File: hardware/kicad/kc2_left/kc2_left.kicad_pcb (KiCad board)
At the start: 2 copper layers, 146.4 x 133.8 mm, 70 parts, among them SW1 KEY_01, SW10 KEY_10, SW11 KEY_11, SW12 KEY_12, SW13 KEY_13, SW14 KEY_14, SW15 KEY_15, SW16 KEY_16, SW17 KEY_17, SW18 KEY_18, SW19 KEY_19, SW2 KEY_02, SW20 KEY_20, SW21 KEY_21, SW22 KEY_22, SW23 KEY_23, SW24 KEY_24, SW25 KEY_25, SW26 KEY_26, SW27 KEY_27, SW28 KEY_28, SW29 KEY_29, SW3 KEY_03, SW30 KEY_30, SW4 KEY_04, SW5 KEY_05, SW6 KEY_06, SW7 KEY_07, SW8 KEY_08, SW9 KEY_09, U1 nice!nano_v2_socket_24pin

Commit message: Finalize KC2 routed PCB draft
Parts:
- moved H3 1.00 mm to (115.4, 44.0)
- moved H4 1.00 mm to (151.4, 44.0)
- moved J_PWR1 1.00 mm to (105.4, 50.0)
- moved SW_RST1 1.00 mm to (123.5, 62.1)
- moved U1 1.00 mm to (133.4, 49.0)
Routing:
- net L_COL3: track 176.2 -> 146.8 mm, vias 1 -> 0
- net L_COL2: track 190.5 -> 165.8 mm, vias 1 -> 0
- net L_COL0: track 219.3 -> 195.5 mm, vias 1 -> 0
- net L_ROW2: track 177.0 -> 157.6 mm, vias 7 -> 1
- net L_ROW0: track 149.6 -> 131.4 mm, vias 7 -> 0
- net L_COL1: track 208.7 -> 191.7 mm
- net L_ROW3: track 199.7 -> 184.4 mm, vias 6 -> 1
- net L_COL4: track 152.7 -> 139.1 mm, vias 1 -> 0
- net L_COL5: track 126.4 -> 112.9 mm
- net L_ROW1: track 150.2 -> 137.0 mm, vias 6 -> 1
- net L_ROW4: track 203.9 -> 211.2 mm, vias 6 -> 1
- net LK15_D: track 15.4 -> 12.0 mm, vias 1 -> 0
- net L_COL6: track 53.5 -> 50.3 mm
- net LK30_D: track 12.0 -> 15.0 mm, vias 0 -> 1
- net LK23_D: track 12.0 -> 13.6 mm
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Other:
- outline, holes or cut-outs redrawn

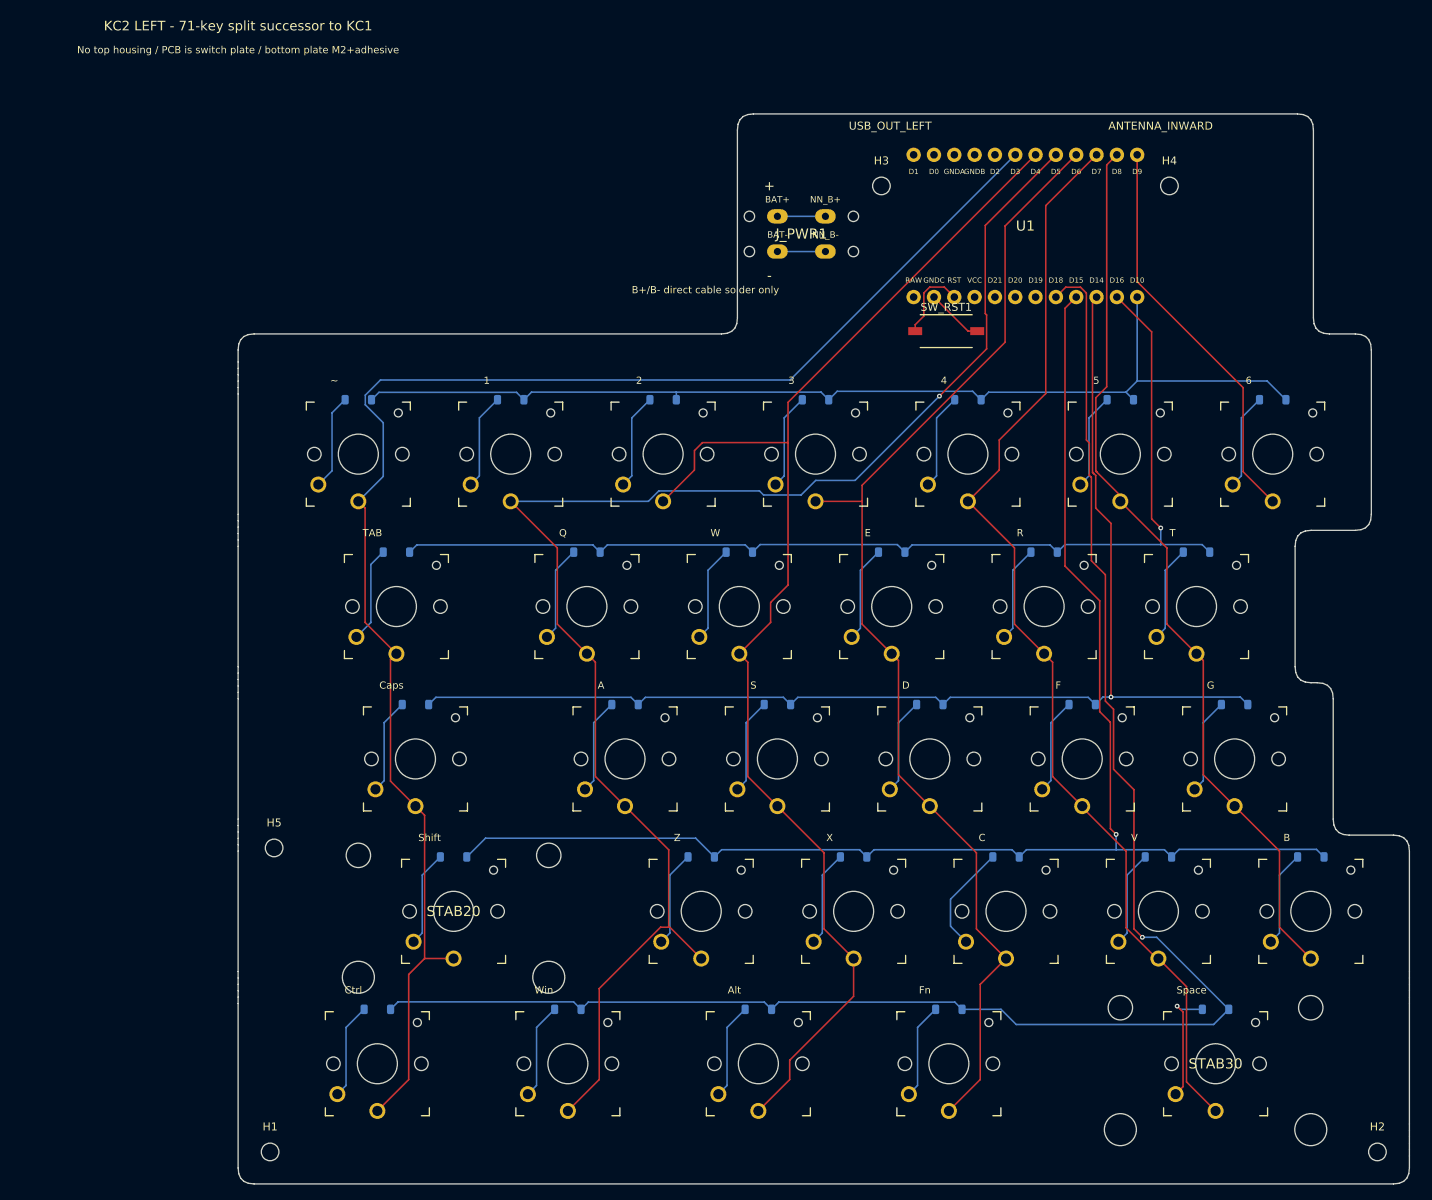
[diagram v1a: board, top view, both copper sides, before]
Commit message: chore: OPS-ARCH-002 KC2 X3 KiCad 산출물을 main 경로로 승격한다
- X3 좌우 프로젝트를 hardware/kicad/kc2_left, hardware/kicad/kc2_right로 승격
- soldered, hotswap, x1, x2 변형은 hardware/kicad/draft 아래에 보존
- manifest, autoroute, file naming, fabrication ZIP, renders, verify scripts를 main 경로 기준으로 갱신
- SRS evidence와 OPS-ARCH-002 verified 상태를 반영
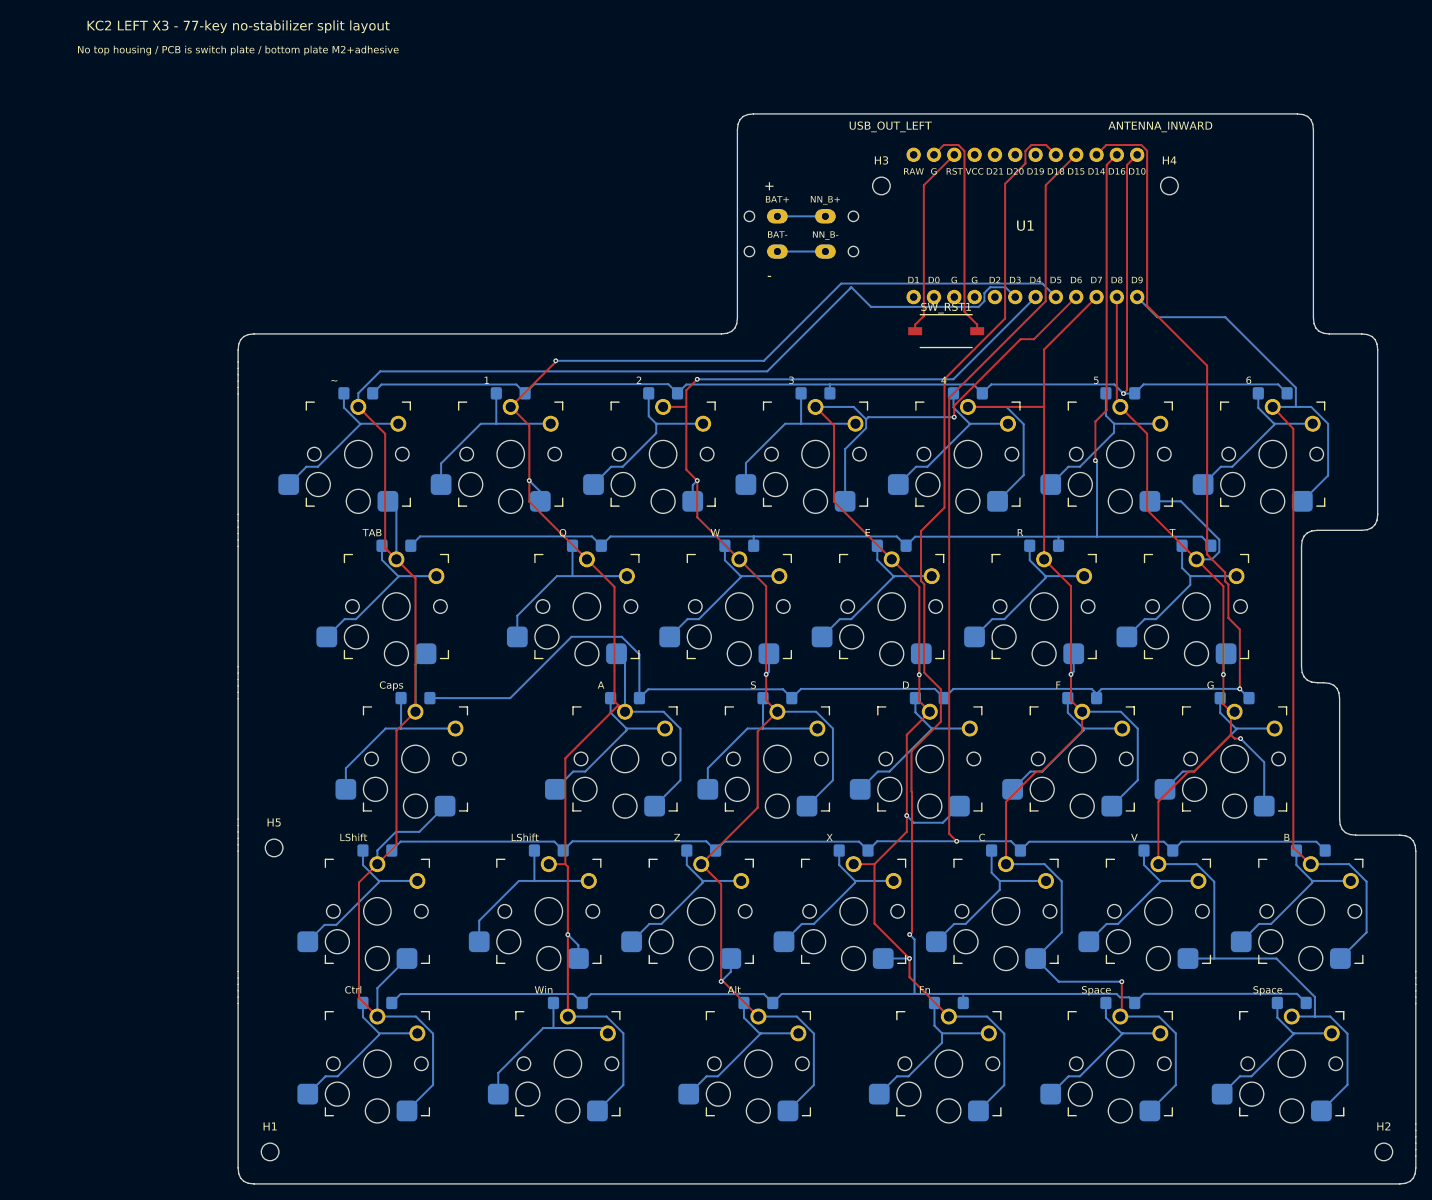
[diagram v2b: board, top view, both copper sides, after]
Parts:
- removed STAB20, STAB30: PCB_mount_stab_for_2.25u, KC2:PCB_Mount_2u_Stabilizer_NPTH
- added D31: 1N4148W_SOD123_DeviceMart_14592018, D_SOD123_HandSolder_14592018, B.Cu at (145.3, 146.1)
- added D32: 1N4148W_SOD123_DeviceMart_14592018, D_SOD123_HandSolder_14592018, B.Cu at (166.7, 146.1)
- added SW31: KEY_31, SW_Kailh_Choc_V1_HotSwap_THT, F.Cu at (145.3, 153.7)
- added SW32: KEY_32, SW_Kailh_Choc_V1_HotSwap_THT, F.Cu at (166.7, 153.7)
- D1, D10, D11, D12, D13, D14, D15, D16, D17, D18, D19, D2, D20, D21, D22, D23, D24, D25, D26, D27, D28, D29, D3, D30, D4, D5, D6, D7, D8, D9: value 1N4148W_SOD-123 -> 1N4148W_SOD123_DeviceMart_14592018; footprint D_SOD-123 -> D_SOD123_HandSolder_14592018
- SW1, SW10, SW11, SW12, SW13, SW14, SW15, SW16, SW17, SW18, SW19, SW2, SW20, SW21, SW22, SW23, SW24, SW25, SW26, SW27, SW28, SW29, SW3, SW30, SW4, SW5, SW6, SW7, SW8, SW9: footprint SW_Kailh_Choc_V1V2_THT_Hybrid -> SW_Kailh_Choc_V1_HotSwap_THT
- U1: footprint KC2:NiceNanoV2_Socket_24Pin -> KC2:NiceNanoV2_Socket_24Pin_USB_OUT_LEFT
- moved D26 118.4 mm to (169.1, 127.1)
- moved SW26 118.2 mm to (169.1, 134.7)
- moved D30 33.3 mm to (123.8, 146.1)
- moved SW30 33.3 mm to (123.8, 153.7)
- moved D27 23.8 mm to (52.4, 146.1)
- moved D28 23.8 mm to (76.2, 146.1)
- moved D29 23.8 mm to (100.0, 146.1)
- moved SW27 23.8 mm to (52.4, 153.7)
- moved SW28 23.8 mm to (76.2, 153.7)
- moved SW29 23.8 mm to (100.0, 153.7)
- moved D23 19.1 mm to (111.9, 127.1)
- moved D25 19.1 mm to (150.0, 127.1)
- moved D21 19.1 mm to (73.8, 127.1)
- moved D22 19.1 mm to (92.9, 127.1)
- moved D24 19.1 mm to (131.0, 127.1)
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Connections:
- D26 pad 1: L_ROW4 -> L_ROW3
- SW26 pad 1: L_COL0 -> L_COL6
- SW27 pad 1: L_COL1 -> L_COL0
- SW28 pad 1: L_COL2 -> L_COL1
- SW29 pad 1: L_COL3 -> L_COL2
- SW30 pad 1: L_COL4 -> L_COL3
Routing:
- net L_COL6: track 50.3 -> 123.7 mm
- net L_COL5: track 112.9 -> 167.3 mm, vias 0 -> 2
- net L_COL4: track 139.1 -> 184.0 mm, vias 0 -> 2
- net L_ROW2: track 157.6 -> 195.0 mm
- net L_COL0: track 195.5 -> 231.3 mm
- net L_ROW3: track 184.4 -> 215.0 mm
- net L_COL3: track 146.8 -> 175.8 mm, vias 0 -> 4
- net L_ROW4: track 211.2 -> 237.5 mm
- net L_COL1: track 191.7 -> 215.3 mm, vias 1 -> 3
- net L_COL2: track 165.8 -> 188.1 mm, vias 0 -> 4
- net LK32_D: track 0.00 -> 21.6 mm
- net LK31_D: track 0.00 -> 21.6 mm
- net GND: track 7.19 -> 27.8 mm
- net L_ROW0: track 131.4 -> 150.6 mm, vias 0 -> 1
- net L_ROW1: track 137.0 -> 154.1 mm
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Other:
- board size 146.4 x 133.8 mm -> 147.2 x 133.8 mm
- board text added: "KC2 LEFT X3 - 77-key no-stabilizer split layout"
- board text added: "LShift"
- board text added: "X3: X2 electrical stack, no-stabilizer 77-key split layout"
- board text removed: "KC2 LEFT - 71-key split successor to KC1"
- board text removed: "Shift"

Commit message: fix: KC2 X3 탭 축소로 nice!nano 안테나 keepout 충돌 해소
배터리 carrier 패드와 불필요한 전원 넷을 제거해 컨트롤러 탭을 축소
reset 스위치 위치와 후처리 라우팅을 조정해 nice!nano 안테나 keepout 및 M2 홀 간섭을 해소
검증기, DRC, 렌더, Gerber, JLCPCB ZIP, docs/spec 증거를 갱신
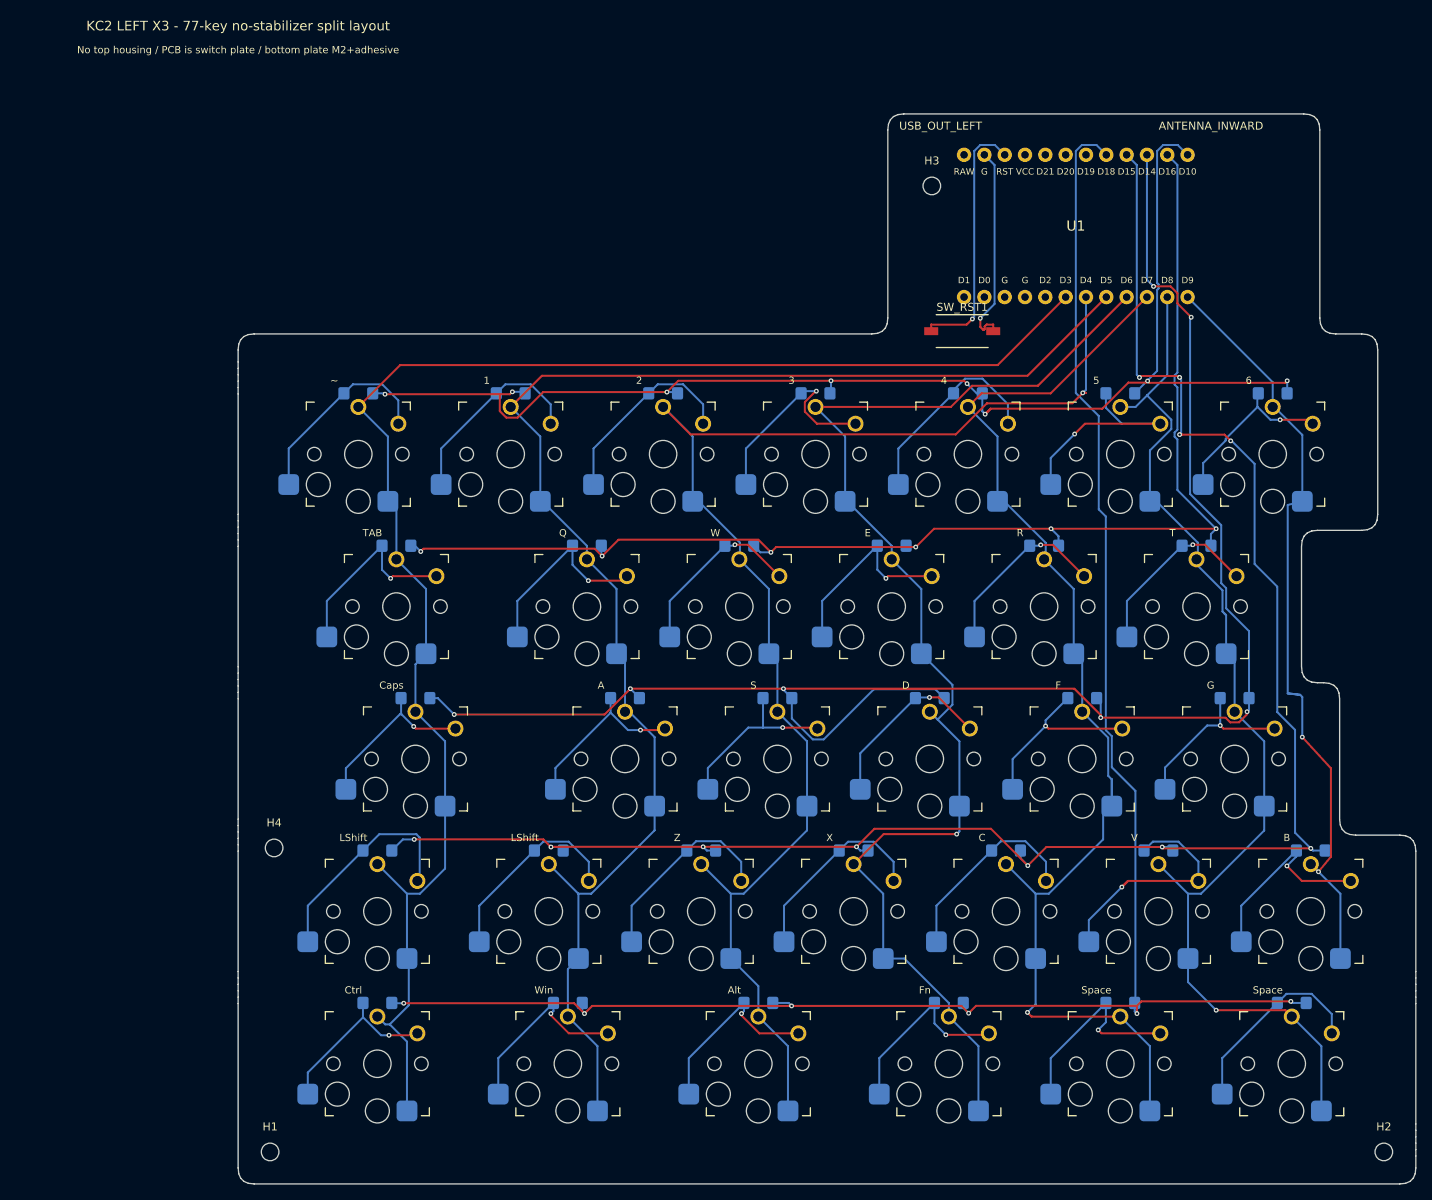
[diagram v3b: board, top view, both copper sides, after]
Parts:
- removed H5: M2_NPTH_2.2, MountingHole_2.2mm_M2
- removed J_PWR1: BAT_NN_direct_solder, KC2:DirectSolderPowerPads
- moved H4 139.2 mm to (39.5, 126.8)
- moved H3 6.30 mm to (121.7, 44.0)
- moved U1 6.30 mm to (139.7, 49.0)
- moved SW_RST1 2.00 mm to (125.5, 62.1)
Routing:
- net L_COL4: track 184.0 -> 150.9 mm, vias 2 -> 1
- net L_COL0: track 231.3 -> 199.8 mm
- net L_COL5: track 167.3 -> 138.0 mm, vias 2 -> 1
- net L_COL1: track 215.3 -> 188.2 mm, vias 3 -> 0
- net L_COL6: track 123.7 -> 97.7 mm, vias 0 -> 2
- net L_ROW3: track 215.0 -> 235.7 mm, vias 1 -> 11
- net L_ROW2: track 195.0 -> 215.0 mm, vias 1 -> 7
- net L_ROW0: track 150.6 -> 169.8 mm, vias 1 -> 8
- net L_COL3: track 175.8 -> 161.9 mm, vias 4 -> 1
- net L_ROW1: track 154.1 -> 164.1 mm, vias 1 -> 6
- net LK25_D: track 21.6 -> 31.3 mm, vias 0 -> 1
- net L_COL2: track 188.1 -> 178.8 mm, vias 4 -> 1
- net RST: track 24.1 -> 32.0 mm, vias 0 -> 1
- net LK06_D: track 21.7 -> 28.2 mm, vias 0 -> 1
- net LK20_D: track 21.6 -> 27.9 mm
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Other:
- outline, holes or cut-outs redrawn
- board text added: "Battery solders directly to nice!nano B+/B-; no carrier power pads"
- board text removed: "+"
- board text removed: "-"
- board text removed: "B+/B- direct cable solder only"
